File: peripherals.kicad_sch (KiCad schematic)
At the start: 57 parts, among them SW1 SW_Push, SW2 SW_Push, U2 ATECC608A-SSHDA, U3 W25Q128JVS

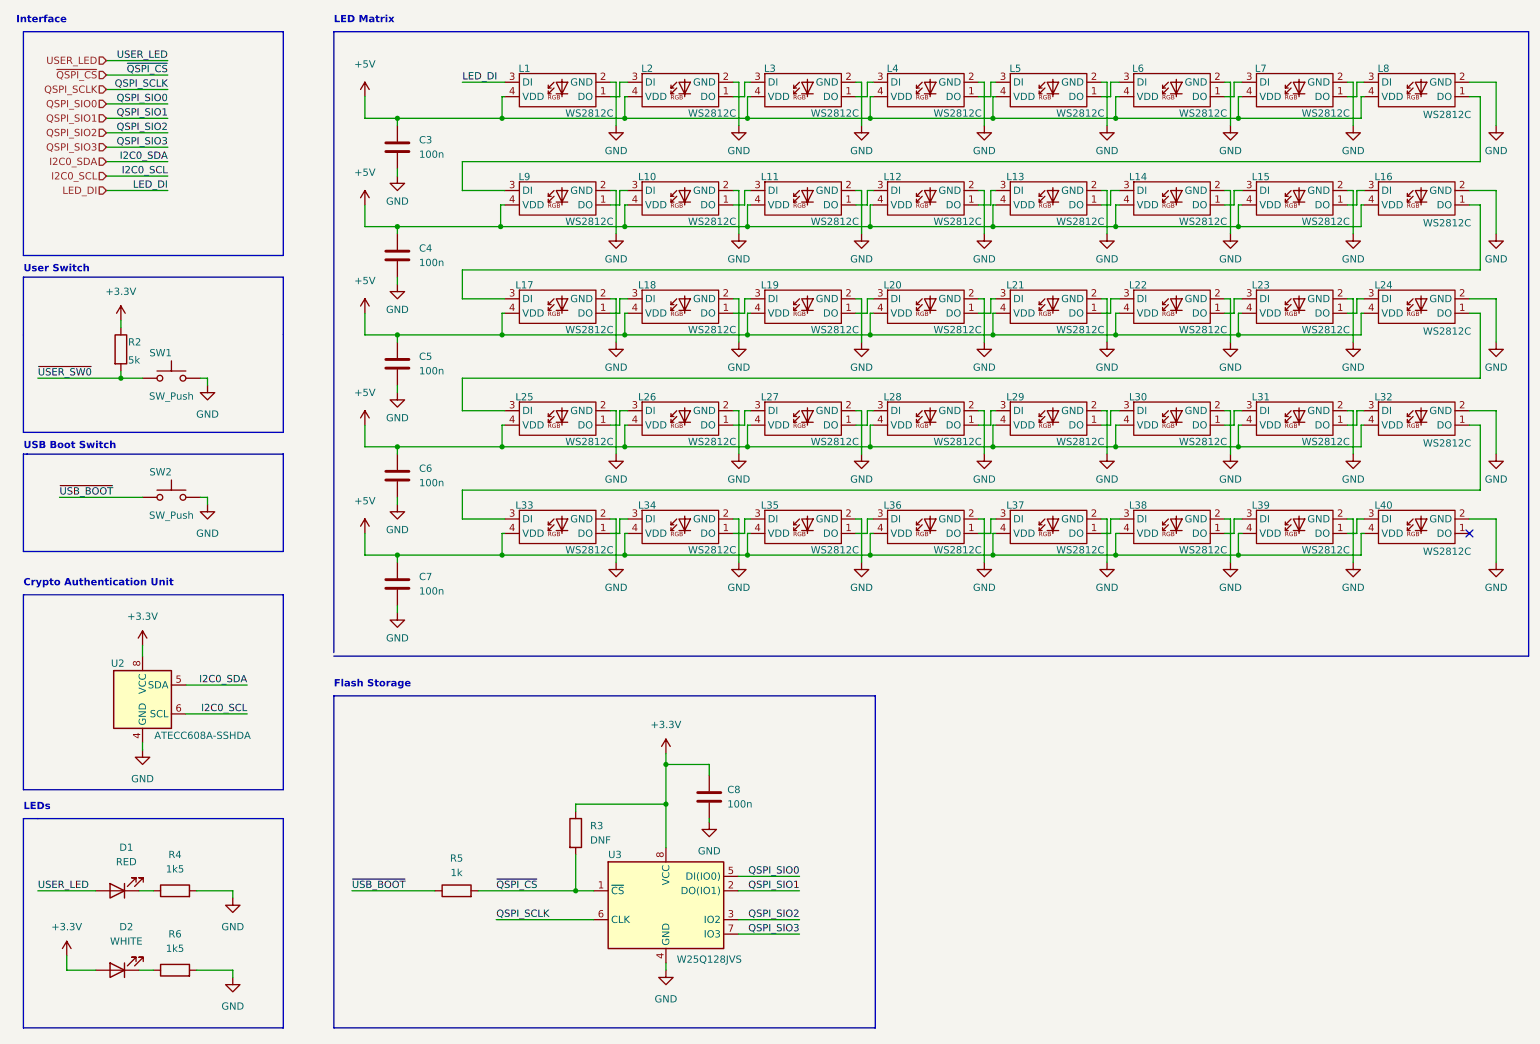
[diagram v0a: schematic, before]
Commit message: Basic routing complete, rename
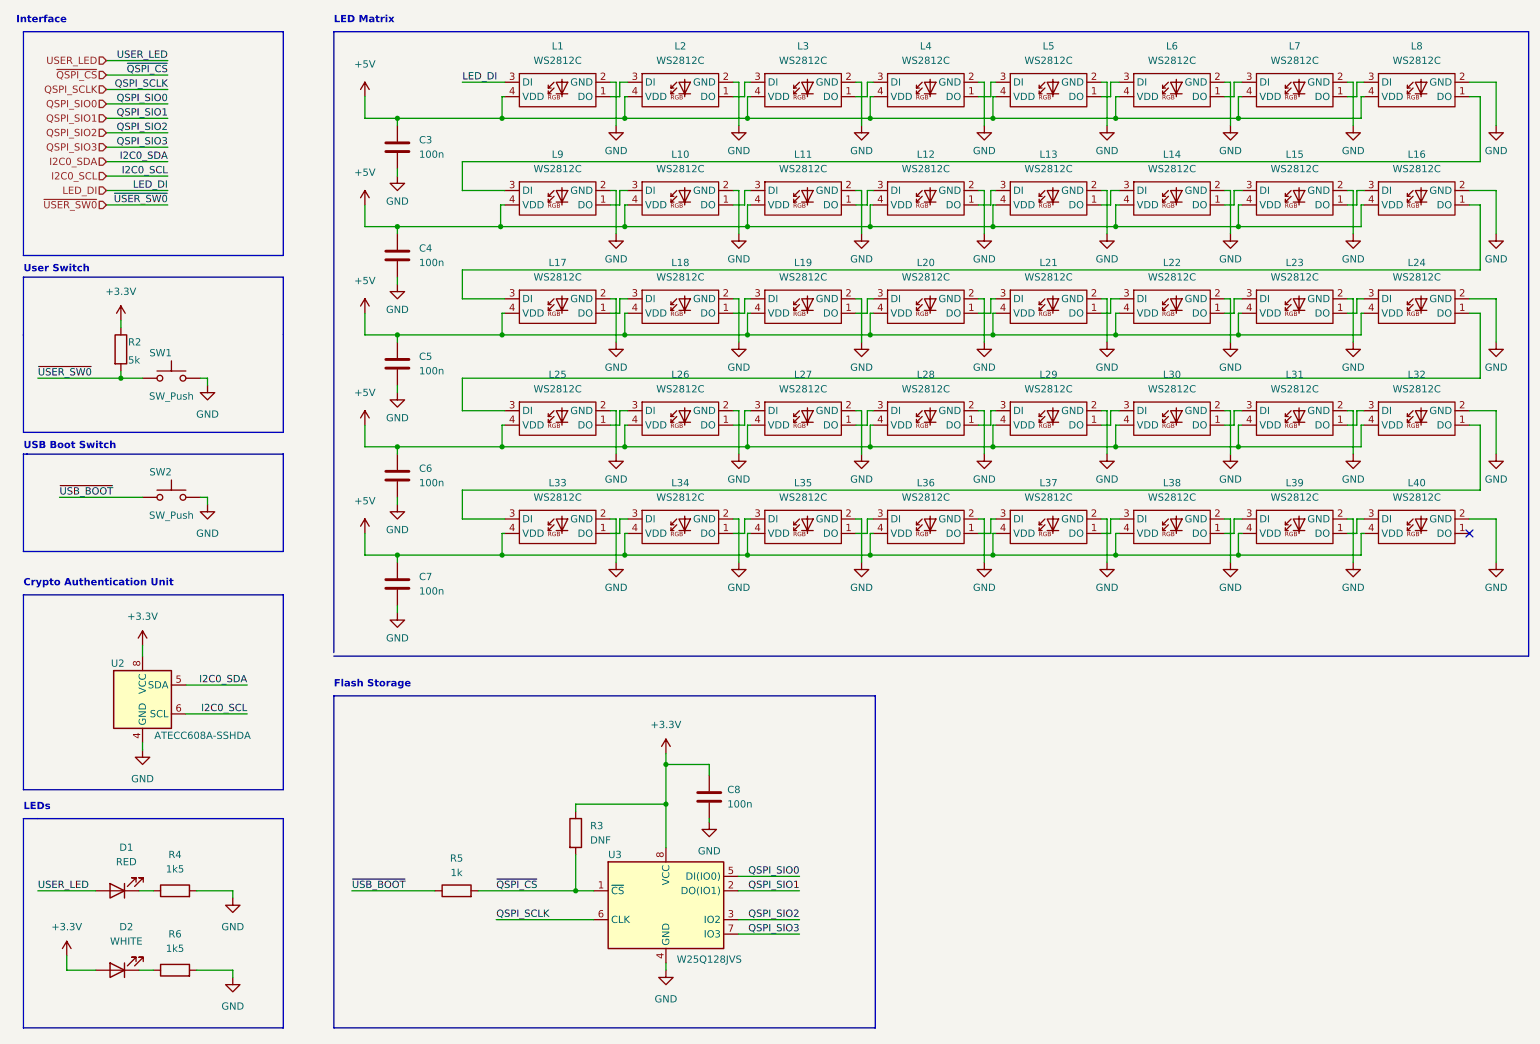
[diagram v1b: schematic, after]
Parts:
- removed L1, L10, L11, L12, L13, L14, L15, L16, L17, L18, L19, L2, L20, L21, L22, L23, L24, L25, L26, L27, L28, L29, L3, L30, L31, L32, L33, L34, L35, L36, L37, L38, L39, L4, L40, L5, L6, L7, L8, L9: WS2812C, pico-card:WS2812C-2020, symbol pico-card:WS2812C
- added L1, L10, L11, L12, L13, L14, L15, L16, L17, L18, L19, L2, L20, L21, L22, L23, L24, L25, L26, L27, L28, L29, L3, L30, L31, L32, L33, L34, L35, L36, L37, L38, L39, L4, L40, L5, L6, L7, L8, L9: WS2812C, Diva-Card:WS2812C-2020, symbol Diva-Card:WS2812C
- SW1, SW2: footprint pico-card:SW_TS-1187A-B-A-B -> Diva-Card:SW_TS-1187A-B-A-B
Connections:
- net +5V: now also L1.4 (VDD), L10.4 (VDD), L11.4 (VDD), L12.4 (VDD), L13.4 (VDD), L14.4 (VDD), L15.4 (VDD), L16.4 (VDD), L17.4 (VDD), L18.4 (VDD), L19.4 (VDD), L2.4 (VDD), L20.4 (VDD), L21.4 (VDD), L22.4 (VDD), L23.4 (VDD), L24.4 (VDD), L25.4 (VDD), L26.4 (VDD), L27.4 (VDD), L28.4 (VDD), L29.4 (VDD), L3.4 (VDD), L30.4 (VDD), L31.4 (VDD), L32.4 (VDD), L33.4 (VDD), L34.4 (VDD), L35.4 (VDD), L36.4 (VDD), L37.4 (VDD), L38.4 (VDD), L39.4 (VDD), L4.4 (VDD), L40.4 (VDD), L5.4 (VDD), L6.4 (VDD), L7.4 (VDD), L8.4 (VDD), L9.4 (VDD)
- net GND: now also L1.2 (GND), L10.2 (GND), L11.2 (GND), L12.2 (GND), L13.2 (GND), L14.2 (GND), L15.2 (GND), L16.2 (GND), L17.2 (GND), L18.2 (GND), L19.2 (GND), L2.2 (GND), L20.2 (GND), L21.2 (GND), L22.2 (GND), L23.2 (GND), L24.2 (GND), L25.2 (GND), L26.2 (GND), L27.2 (GND), L28.2 (GND), L29.2 (GND), L3.2 (GND), L30.2 (GND), L31.2 (GND), L32.2 (GND), L33.2 (GND), L34.2 (GND), L35.2 (GND), L36.2 (GND), L37.2 (GND), L38.2 (GND), L39.2 (GND), L4.2 (GND), L40.2 (GND), L5.2 (GND), L6.2 (GND), L7.2 (GND), L8.2 (GND), L9.2 (GND)
- net LED_DI: now also L1.3 (DI)
- new net: L3.1 (DO), L4.3 (DI)
- new net: L2.1 (DO), L3.3 (DI)
- new net: L38.1 (DO), L39.3 (DI)
- new net: L37.1 (DO), L38.3 (DI)
- new net: L11.1 (DO), L12.3 (DI)
- new net: L10.1 (DO), L11.3 (DI)
- new net: L6.1 (DO), L7.3 (DI)
- new net: L5.1 (DO), L6.3 (DI)
- new net: L4.1 (DO), L5.3 (DI)
- new net: L10.3 (DI), L9.1 (DO)
- new net: L22.1 (DO), L23.3 (DI)
- new net: L21.1 (DO), L22.3 (DI)
- new net: L8.1 (DO), L9.3 (DI)
- new net: L7.1 (DO), L8.3 (DI)
- new net: L34.1 (DO), L35.3 (DI)
- new net: L33.1 (DO), L34.3 (DI)
- new net: L32.1 (DO), L33.3 (DI)
- new net: L35.1 (DO), L36.3 (DI)
- new net: L16.1 (DO), L17.3 (DI)
- new net: L15.1 (DO), L16.3 (DI)
- new net: L1.1 (DO), L2.3 (DI)
- new net: L39.1 (DO), L40.3 (DI)
- new net: L29.1 (DO), L30.3 (DI)
- new net: L28.1 (DO), L29.3 (DI)
- new net: L24.1 (DO), L25.3 (DI)
- new net: L23.1 (DO), L24.3 (DI)
- new net: L31.1 (DO), L32.3 (DI)
- new net: L30.1 (DO), L31.3 (DI)
- new net: L17.1 (DO), L18.3 (DI)
- new net: L13.1 (DO), L14.3 (DI)
- new net: L12.1 (DO), L13.3 (DI)
- new net: L20.1 (DO), L21.3 (DI)
- new net: L19.1 (DO), L20.3 (DI)
- new net: L27.1 (DO), L28.3 (DI)
- new net: L25.1 (DO), L26.3 (DI)
- new net: L26.1 (DO), L27.3 (DI)
- new net: L18.1 (DO), L19.3 (DI)
- new net: L14.1 (DO), L15.3 (DI)
- new net: L36.1 (DO), L37.3 (DI)

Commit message: Adding test gerber and bom
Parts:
- D1: value RED -> EMERALD
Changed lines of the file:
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@@
     (in_bom yes) (on_board yes) (fields_autoplaced)
     (property "Reference" "D1" (id 0) (at 34.6075 162.56 0))
-    (property "Value" "RED" (id 1) (at 34.6075 165.1 0))
+    (property "Value" "EMERALD" (id 1) (at 34.6075 165.1 0))
     (property "Footprint" "LED_SMD:LED_0402_1005Metric" (id 2) (at 33.02 170.18 0)
       (effects (font (size 1.27 1.27)) hide)

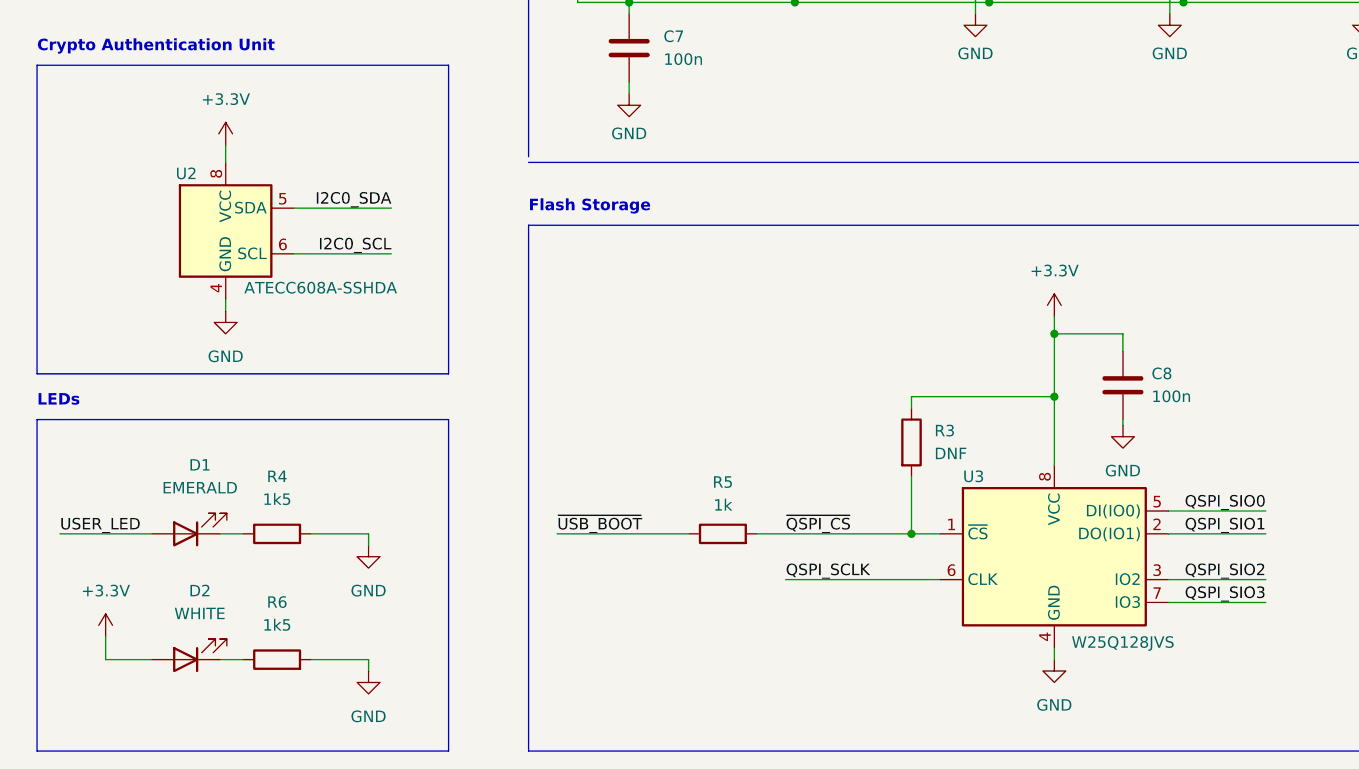
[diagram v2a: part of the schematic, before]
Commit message: updating footprints to udfn
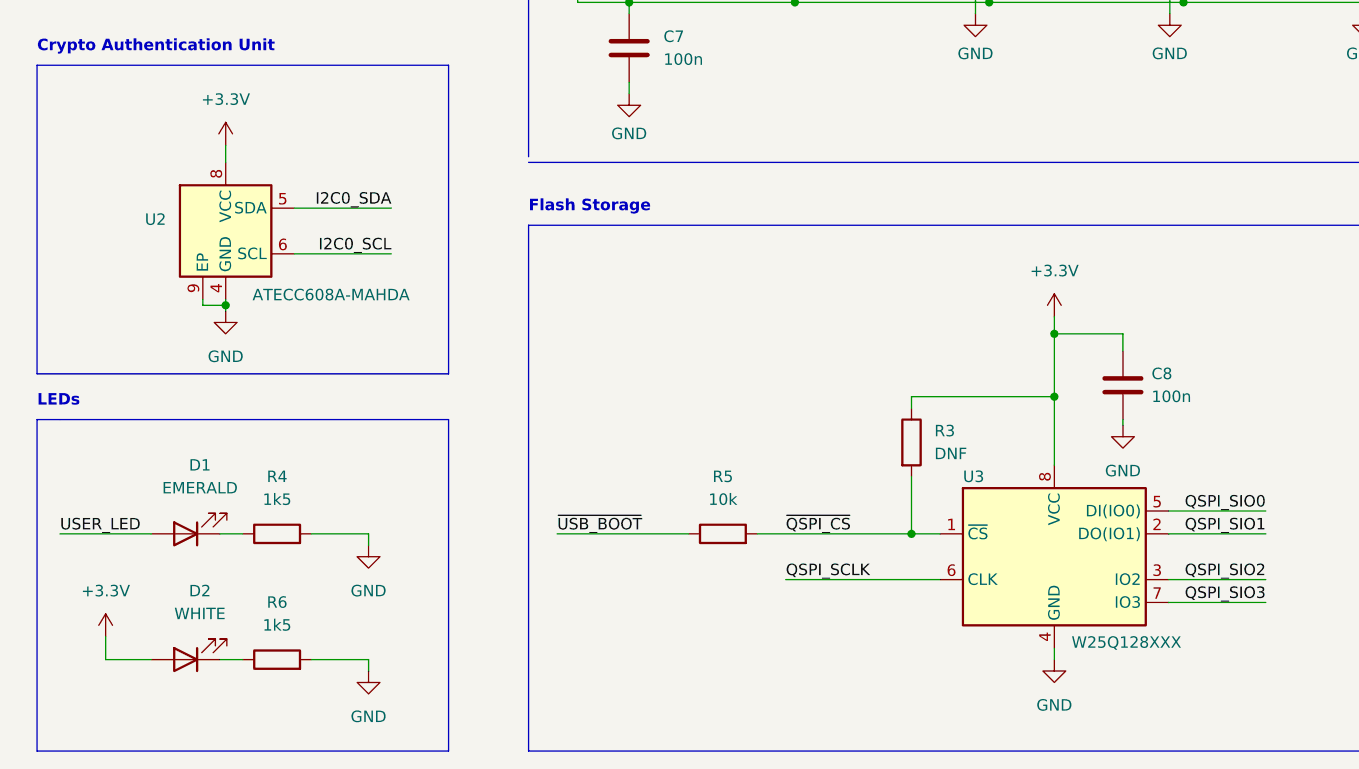
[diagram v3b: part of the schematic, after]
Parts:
- removed U2: ATECC608A-SSHDA, Package_SO:SOIC-8_3.9x4.9mm_P1.27mm, symbol Security:ATECC608A-SSHDA
- added U2: ATECC608A-MAHDA, Package_DFN_QFN:DFN-8-1EP_3x2mm_P0.5mm_EP1.3x1.5mm, symbol Security:ATECC608A-MAHDA
- R5: value 1k -> 10k
- U3: value W25Q128JVS -> W25Q128XXX; footprint Package_SO:SOIC-8_5.23x5.23mm_P1.27mm -> Diva-Card:W25Q128JVPIQ TR
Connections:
- net +3V3: now also U2.8 (VCC)
- net GND: now also U2.4 (GND), U2.9 (EP)
- net I2C0_SCL: now also U2.6 (SCL)
- net I2C0_SDA: now also U2.5 (SDA)

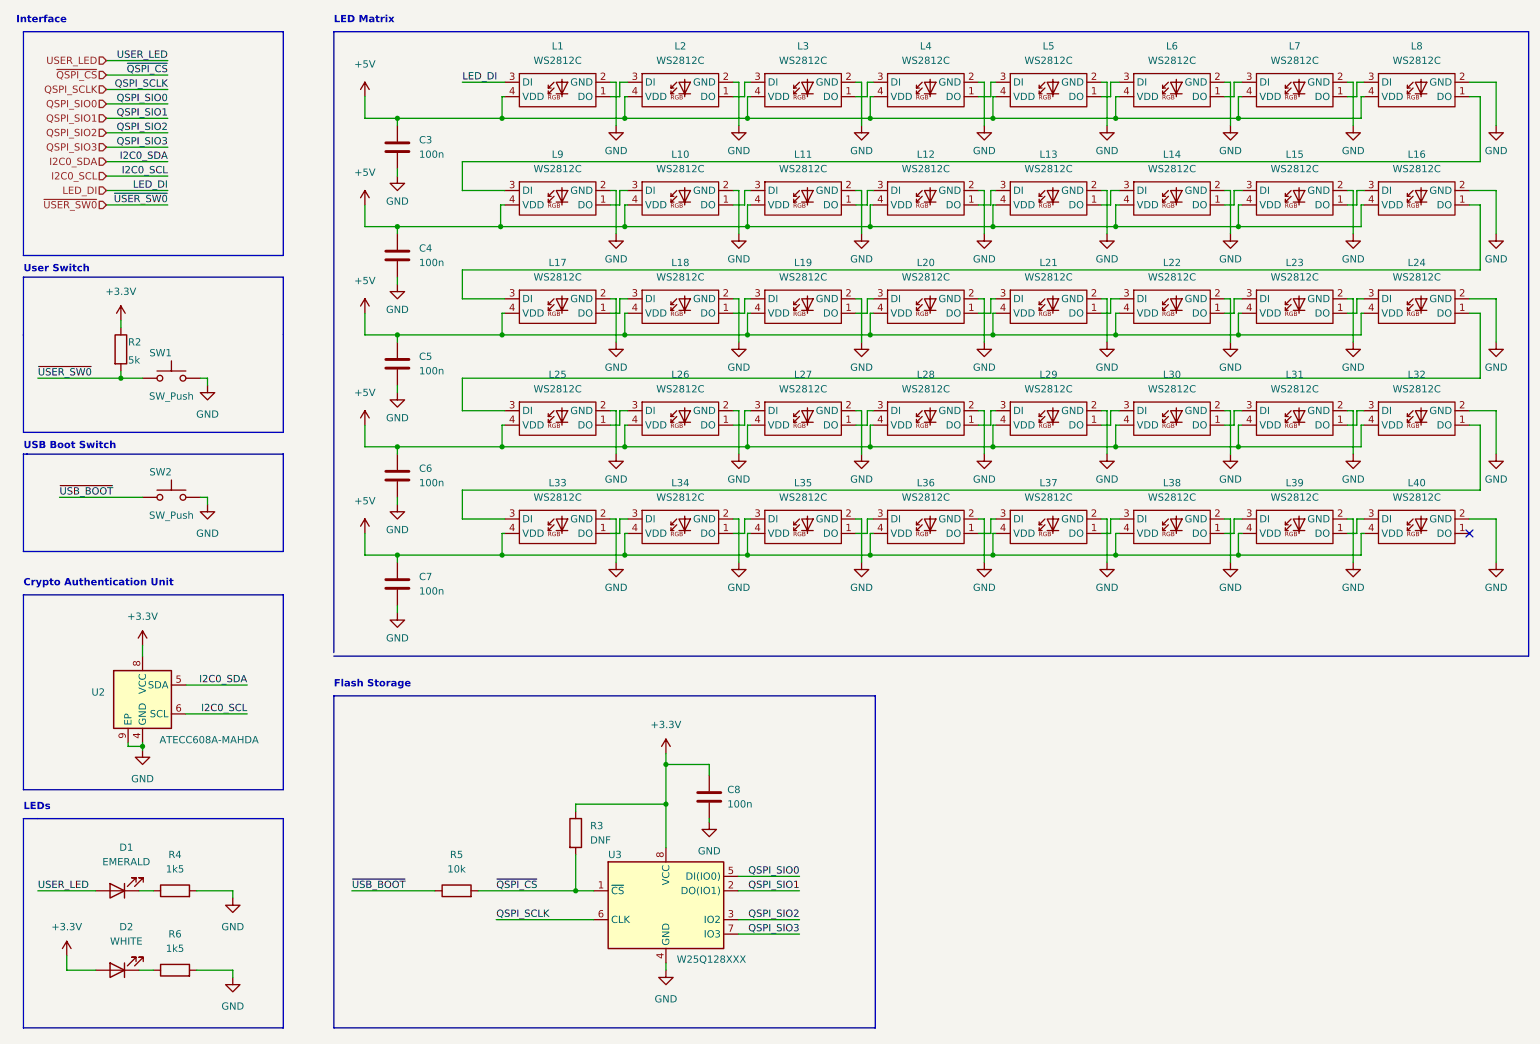
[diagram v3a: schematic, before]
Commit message: Adding schematic pdf
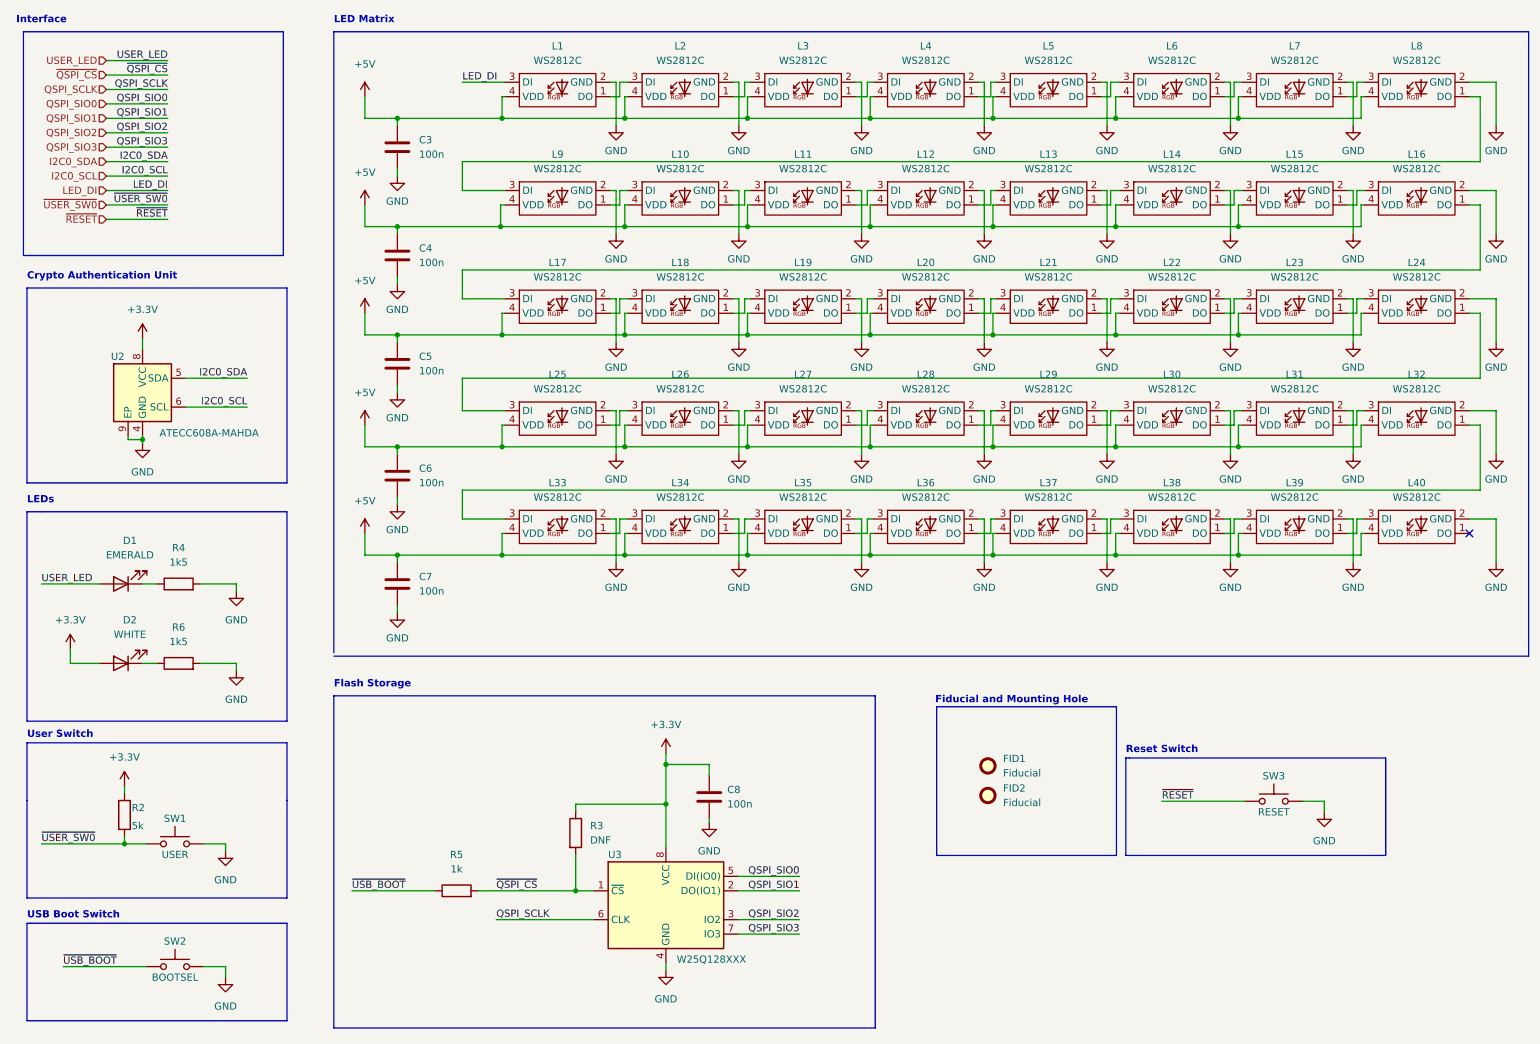
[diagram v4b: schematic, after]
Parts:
- added FID1, FID2: Fiducial, Fiducial:Fiducial_0.5mm_Mask1mm, symbol Mechanical:Fiducial
- added SW3: RESET, Diva-Card:SW_TS-1187A-B-A-B, symbol Switch:SW_Push
- R5: value 10k -> 1k
- SW1: value SW_Push -> USER
- SW2: value SW_Push -> BOOTSEL
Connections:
- net GND: now also SW3.2
- new net ~{RESET}: SW3.1
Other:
- note added: "Fiducial and Mounting Hole"
- note added: "Reset Switch"
- company: (none) -> DIVA ENG
- title: (none) -> Pico Card
- moved on the sheet: D1, D2, R2, R4, R6, SW1, SW2, U2

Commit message: design flaw fix
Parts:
- added C23, C24, C25: 1u, Capacitor_SMD:C_0402_1005Metric, symbol Device:C
- R3: value DNF -> 10k
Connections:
- net GND: now also C23.2, C24.2, C25.2
- net ~{QSPI_CS}: now also C25.1
- net ~{RESET}: now also C23.1
- net ~{USER_SW0}: now also C24.1
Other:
- moved on the sheet: D1, D2, R2, R4, R5, R6, SW1, SW3, U2
